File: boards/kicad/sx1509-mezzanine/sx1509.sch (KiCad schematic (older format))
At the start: 19 parts, among them J1 Conn_02x08_Odd_Even, J2 Conn_02x08_Odd_Even, J3 Conn_01x02_Male, J4 Conn_01x02_Male, P1 CONN_02X20, P2 CONN_02X20, U1 SX1509

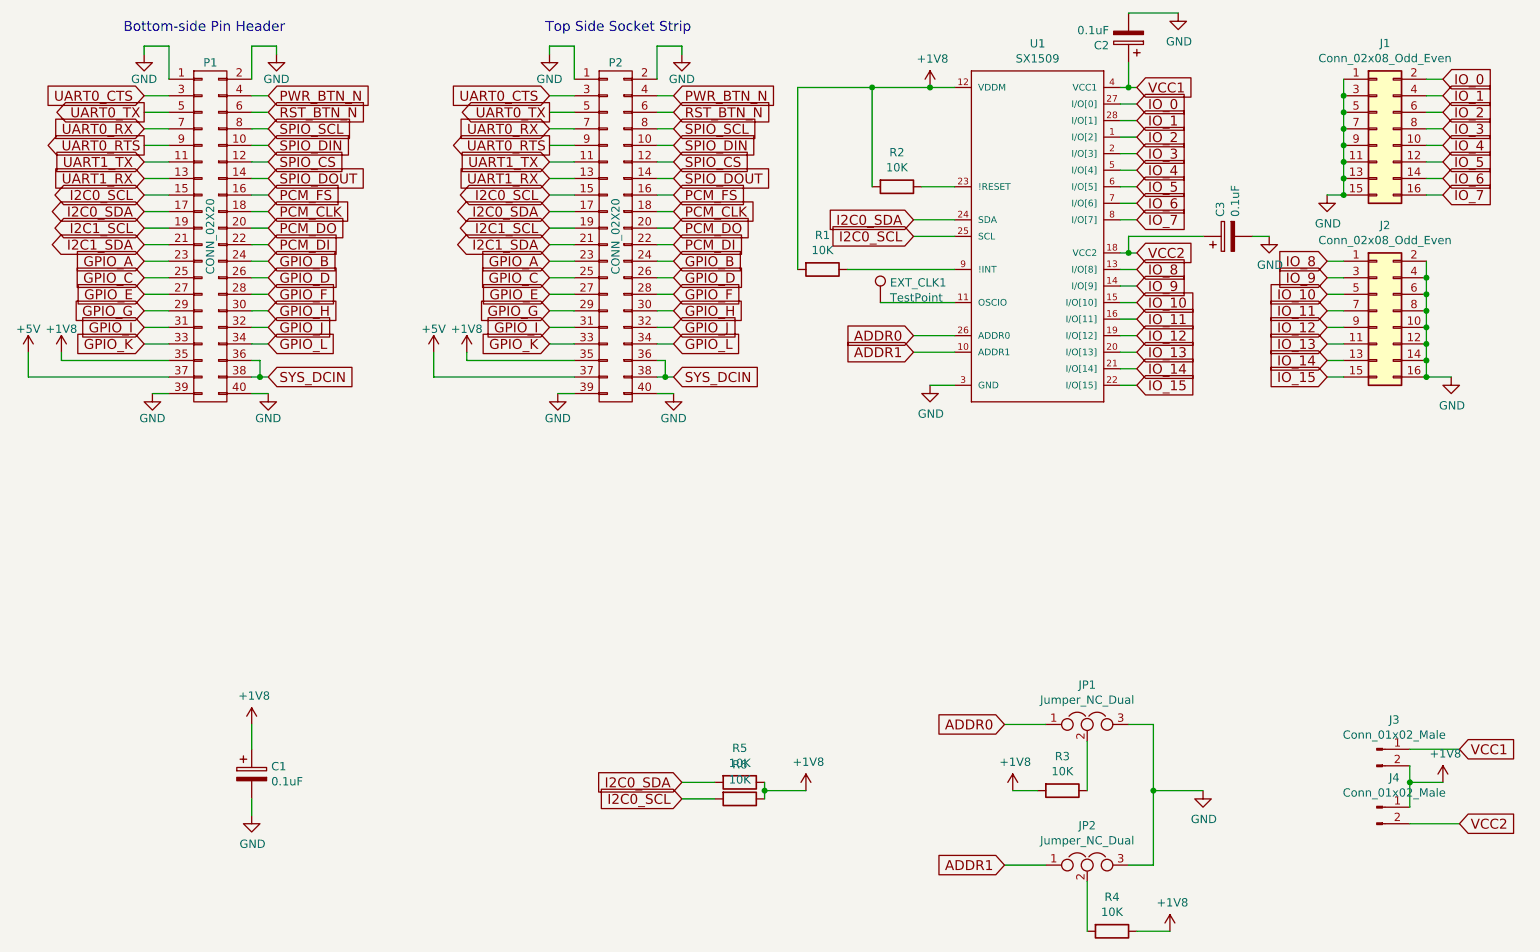
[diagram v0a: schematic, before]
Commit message: Clean up design
The placement, routing, and silkscreen were updated to look nicer.
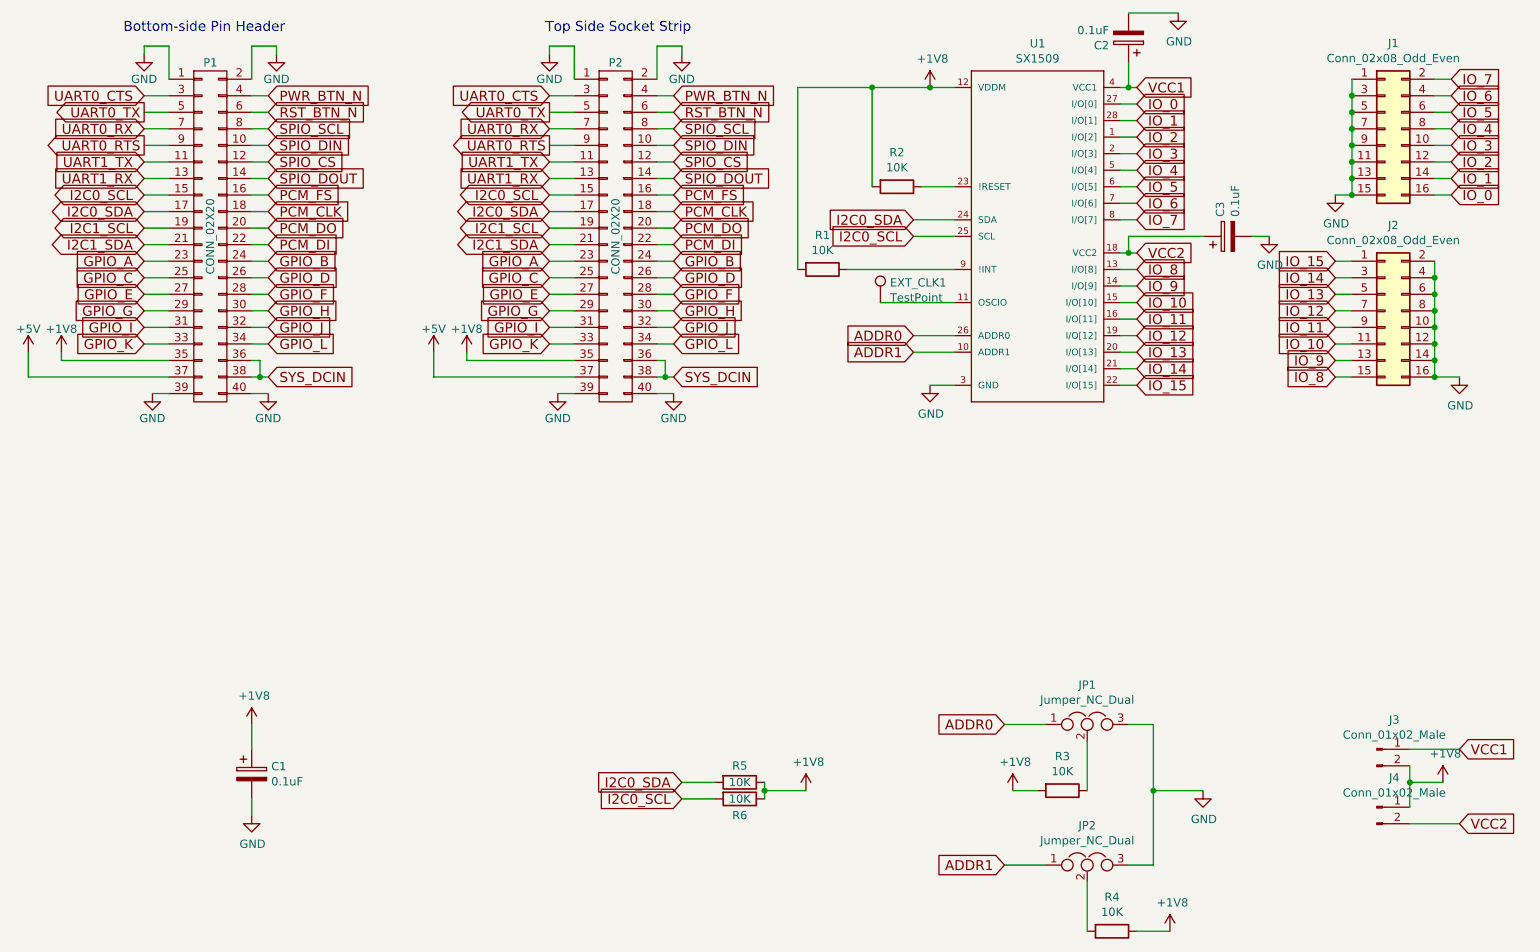
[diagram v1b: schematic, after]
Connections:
- net IO_0: now also J1.16 (Pin_16); no longer J1.2 (Pin_2)
- net IO_1: now also J1.14 (Pin_14); no longer J1.4 (Pin_4)
- net IO_10: now also J2.11 (Pin_11); no longer J2.5 (Pin_5)
- net IO_11: now also J2.9 (Pin_9); no longer J2.7 (Pin_7)
- net IO_12: now also J2.7 (Pin_7); no longer J2.9 (Pin_9)
- net IO_13: now also J2.5 (Pin_5); no longer J2.11 (Pin_11)
- net IO_14: now also J2.3 (Pin_3); no longer J2.13 (Pin_13)
- net IO_15: now also J2.1 (Pin_1); no longer J2.15 (Pin_15)
- net IO_2: now also J1.12 (Pin_12); no longer J1.6 (Pin_6)
- net IO_3: now also J1.10 (Pin_10); no longer J1.8 (Pin_8)
- net IO_4: now also J1.8 (Pin_8); no longer J1.10 (Pin_10)
- net IO_5: now also J1.6 (Pin_6); no longer J1.12 (Pin_12)
- net IO_6: now also J1.4 (Pin_4); no longer J1.14 (Pin_14)
- net IO_7: now also J1.2 (Pin_2); no longer J1.16 (Pin_16)
- net IO_8: now also J2.15 (Pin_15); no longer J2.1 (Pin_1)
- net IO_9: now also J2.13 (Pin_13); no longer J2.3 (Pin_3)
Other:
- moved on the sheet: J1, J2
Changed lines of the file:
@@
 EESchema Schematic File Version 4
 LIBS:sx1509-cache
-EELAYER 29 0
+EELAYER 26 0
 EELAYER END
 $Descr A4 11693 8268
@@
 Text GLabel 7500 2950 2    60   Input ~ 0
 IO_15
-Text GLabel 9350 1100 2    60   Input ~ 0
+Text GLabel 9400 1800 2    60   Input ~ 0
 IO_0
-Text GLabel 9350 1200 2    60   Input ~ 0
+Text GLabel 9400 1700 2    60   Input ~ 0
 IO_1
-Text GLabel 9350 1300 2    60   Input ~ 0
+Text GLabel 9400 1600 2    60   Input ~ 0
 IO_2
-Text GLabel 9350 1400 2    60   Input ~ 0
+Text GLabel 9400 1500 2    60   Input ~ 0
 IO_3
-Text GLabel 9350 1500 2    60   Input ~ 0
+Text GLabel 9400 1400 2    60   Input ~ 0
 IO_4
-Text GLabel 9350 1600 2    60   Input ~ 0
+Text GLabel 9400 1300 2    60   Input ~ 0
 IO_5
-Text GLabel 9350 1700 2    60   Input ~ 0
+Text GLabel 9400 1200 2    60   Input ~ 0
 IO_6
-Text GLabel 9350 1800 2    60   Input ~ 0
+Text GLabel 9400 1100 2    60   Input ~ 0
 IO_7
-Text GLabel 8650 2200 0    60   Input ~ 0
+Text GLabel 8700 2900 0    60   Input ~ 0
 IO_8
-Text GLabel 8650 2300 0    60   Input ~ 0
+Text GLabel 8700 2800 0    60   Input ~ 0
 IO_9
-Text GLabel 8650 2400 0    60   Input ~ 0
+Text GLabel 8700 2700 0    60   Input ~ 0
 IO_10
-Text GLabel 8650 2500 0    60   Input ~ 0
+Text GLabel 8700 2600 0    60   Input ~ 0
 IO_11
-Text GLabel 8650 2600 0    60   Input ~ 0
+Text GLabel 8700 2500 0    60   Input ~ 0
 IO_12
-Text GLabel 8650 2700 0    60   Input ~ 0
+Text GLabel 8700 2400 0    60   Input ~ 0
 IO_13
-Text GLabel 8650 2800 0    60   Input ~ 0
+Text GLabel 8700 2300 0    60   Input ~ 0
 IO_14
-Text GLabel 8650 2900 0    60   Input ~ 0
+Text GLabel 8700 2200 0    60   Input ~ 0
 IO_15
 Wire Wire Line
@@
 U 1 1 5C81D9F5
 P 5100 5350
-F 0 "R5" V 4893 5350 50  0000 C CNN
-F 1 "10K" V 4984 5350 50  0000 C CNN
+F 0 "R5" V 5000 5350 50  0000 C CNN
+F 1 "10K" V 5100 5350 50  0000 C CNN
 F 2 "Resistor_SMD:R_0201_0603Metric" V 5030 5350 50  0001 C CNN
 F 3 "~" H 5100 5350 50  0001 C CNN
@@
 U 1 1 5C827A9C
 P 5100 5450
-F 0 "R6" V 4893 5450 50  0000 C CNN
-F 1 "10K" V 4984 5450 50  0000 C CNN
+F 0 "R6" V 5200 5450 50  0000 C CNN
+F 1 "10K" V 5100 5450 50  0000 C CNN
 F 2 "Resistor_SMD:R_0201_0603Metric" V 5030 5450 50  0001 C CNN
 F 3 "~" H 5100 5450 50  0001 C CNN
@@
 	5950 2450 6400 2450
 Wire Wire Line
-	9350 1100 9250 1100
-Wire Wire Line
-	9250 1200 9350 1200
-Wire Wire Line
-	9350 1300 9250 1300
-Wire Wire Line
-	9250 1400 9350 1400
-Wire Wire Line
-	9350 1500 9250 1500
-Wire Wire Line
-	9250 1600 9350 1600
-Wire Wire Line
-	9250 1700 9350 1700
-Wire Wire Line
-	9250 1800 9350 1800
-Wire Wire Line
-	8750 2900 8650 2900
-Wire Wire Line
-	8750 2800 8650 2800
-Wire Wire Line
-	8750 2700 8650 2700
-Wire Wire Line
-	8750 2600 8650 2600
-Wire Wire Line
-	8750 2500 8650 2500
-Wire Wire Line
-	8750 2400 8650 2400
-Wire Wire Line
-	8750 2300 8650 2300
-Wire Wire Line
-	8750 2200 8650 2200
+	9400 1100 9300 1100
+Wire Wire Line
+	9300 1200 9400 1200
+Wire Wire Line
+	9400 1300 9300 1300
+Wire Wire Line
+	9300 1400 9400 1400
+Wire Wire Line
+	9400 1500 9300 1500
+Wire Wire Line
+	9300 1600 9400 1600
+Wire Wire Line
+	9300 1700 9400 1700
+Wire Wire Line
+	9300 1800 9400 1800
+Wire Wire Line
+	8800 2900 8700 2900
+Wire Wire Line
+	8800 2800 8700 2800
+Wire Wire Line
+	8800 2700 8700 2700
+Wire Wire Line
+	8800 2600 8700 2600
+Wire Wire Line
+	8800 2500 8700 2500
+Wire Wire Line
+	8800 2400 8700 2400
+Wire Wire Line
+	8800 2300 8700 2300
+Wire Wire Line
+	8800 2200 8700 2200
 $Comp
 L power:GND #PWR0112
 U 1 1 5C80488A
-P 8650 1800
-F 0 "#PWR0112" H 8650 1550 50  0001 C CNN
-F 1 "GND" H 8655 1627 50  0000 C CNN
-F 2 "" H 8650 1800 50  0001 C CNN
-F 3 "" H 8650 1800 50  0001 C CNN
-	1    8650 1800
-	1    0    0    -1
-$EndComp
-Wire Wire Line
-	8650 1800 8750 1800
+P 8700 1800
+F 0 "#PWR0112" H 8700 1550 50  0001 C CNN
+F 1 "GND" H 8705 1627 50  0000 C CNN
+F 2 "" H 8700 1800 50  0001 C CNN
+F 3 "" H 8700 1800 50  0001 C CNN
+	1    8700 1800
+	1    0    0    -1
+$EndComp
+Wire Wire Line
+	8700 1800 8800 1800
 $Comp
 L power:GND #PWR0113
 U 1 1 5C897F94
-P 9400 2900
-F 0 "#PWR0113" H 9400 2650 50  0001 C CNN
-F 1 "GND" H 9405 2727 50  0000 C CNN
-F 2 "" H 9400 2900 50  0001 C CNN
-F 3 "" H 9400 2900 50  0001 C CNN
-	1    9400 2900
-	1    0    0    -1
-$EndComp
-Wire Wire Line
-	9250 2900 9400 2900
+P 9450 2900
+F 0 "#PWR0113" H 9450 2650 50  0001 C CNN
+F 1 "GND" H 9455 2727 50  0000 C CNN
+F 2 "" H 9450 2900 50  0001 C CNN
+F 3 "" H 9450 2900 50  0001 C CNN
+	1    9450 2900
+	1    0    0    -1
+$EndComp
+Wire Wire Line
+	9300 2900 9450 2900
 Wire Wire Line
 	2150 5550 2150 5450
@@
 L Connector_Generic:Conn_02x08_Odd_Even J1
 U 1 1 5C7E8971
-P 8950 1400
-F 0 "J1" H 9000 1917 50  0000 C CNN
-F 1 "Conn_02x08_Odd_Even" H 9000 1826 50  0000 C CNN
-F 2 "Connector_PinHeader_2.54mm:PinHeader_2x08_P2.54mm_Horizontal" H 8950 1400 50  0001 C CNN
-F 3 "~" H 8950 1400 50  0001 C CNN
-	1    8950 1400
+P 9000 1400
+F 0 "J1" H 9050 1917 50  0000 C CNN
+F 1 "Conn_02x08_Odd_Even" H 9050 1826 50  0000 C CNN
+F 2 "Connector_PinHeader_2.54mm:PinHeader_2x08_P2.54mm_Horizontal" H 9000 1400 50  0001 C CNN
+F 3 "~" H 9000 1400 50  0001 C CNN
+	1    9000 1400
 	1    0    0    -1
 $EndComp
@@
 L Connector_Generic:Conn_02x08_Odd_Even J2
 U 1 1 5C7E8A64
-P 8950 2500
-F 0 "J2" H 9000 3017 50  0000 C CNN
-F 1 "Conn_02x08_Odd_Even" H 9000 2926 50  0000 C CNN
-F 2 "Connector_PinHeader_2.54mm:PinHeader_2x08_P2.54mm_Horizontal" H 8950 2500 50  0001 C CNN
-F 3 "~" H 8950 2500 50  0001 C CNN
-	1    8950 2500
-	1    0    0    -1
-$EndComp
-Wire Wire Line
-	8750 1700 8750 1800
-Connection ~ 8750 1800
-Wire Wire Line
-	9250 2800 9250 2900
-Connection ~ 9250 2900
-Wire Wire Line
-	8750 1700 8750 1600
-Connection ~ 8750 1700
-Connection ~ 8750 1200
-Wire Wire Line
-	8750 1200 8750 1100
-Connection ~ 8750 1300
-Wire Wire Line
-	8750 1300 8750 1200
-Connection ~ 8750 1400
-Wire Wire Line
-	8750 1400 8750 1300
-Connection ~ 8750 1500
-Wire Wire Line
-	8750 1500 8750 1400
-Connection ~ 8750 1600
-Wire Wire Line
-	8750 1600 8750 1500
-Wire Wire Line
-	9250 2200 9250 2300
-Connection ~ 9250 2800
-Connection ~ 9250 2300
-Wire Wire Line
-	9250 2300 9250 2400
-Connection ~ 9250 2400
-Wire Wire Line
-	9250 2400 9250 2500
-Connection ~ 9250 2500
-Wire Wire Line
-	9250 2500 9250 2600
-Connection ~ 9250 2600
-Wire Wire Line
-	9250 2600 9250 2700
-Connection ~ 9250 2700
-Wire Wire Line
-	9250 2700 9250 2800
+P 9000 2500
+F 0 "J2" H 9050 3017 50  0000 C CNN
+F 1 "Conn_02x08_Odd_Even" H 9050 2926 50  0000 C CNN
+F 2 "Connector_PinHeader_2.54mm:PinHeader_2x08_P2.54mm_Horizontal" H 9000 2500 50  0001 C CNN
+F 3 "~" H 9000 2500 50  0001 C CNN
+	1    9000 2500
+	1    0    0    -1
+$EndComp
+Wire Wire Line
+	8800 1700 8800 1800
+Connection ~ 8800 1800
+Wire Wire Line
+	9300 2800 9300 2900
+Connection ~ 9300 2900
+Wire Wire Line
+	8800 1700 8800 1600
+Connection ~ 8800 1700
+Connection ~ 8800 1200
+Wire Wire Line
+	8800 1200 8800 1100
+Connection ~ 8800 1300
+Wire Wire Line
+	8800 1300 8800 1200
+Connection ~ 8800 1400
+Wire Wire Line
+	8800 1400 8800 1300
+Connection ~ 8800 1500
+Wire Wire Line
+	8800 1500 8800 1400
+Connection ~ 8800 1600
+Wire Wire Line
+	8800 1600 8800 1500
+Wire Wire Line
+	9300 2200 9300 2300
+Connection ~ 9300 2800
+Connection ~ 9300 2300
+Wire Wire Line
+	9300 2300 9300 2400
+Connection ~ 9300 2400
+Wire Wire Line
+	9300 2400 9300 2500
+Connection ~ 9300 2500
+Wire Wire Line
+	9300 2500 9300 2600
+Connection ~ 9300 2600
+Wire Wire Line
+	9300 2600 9300 2700
+Connection ~ 9300 2700
+Wire Wire Line
+	9300 2700 9300 2800
 $EndSCHEMATC
